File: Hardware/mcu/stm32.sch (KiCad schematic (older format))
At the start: 37 parts, among them P1101 EXP1, P1102 EXP2, P1103 EXP3, P1104 EXP4, P1105 EXPPWR, P901 EXP5, Q1101 NPN, SW1101 Reset, U1101 STM32F103ZC, U903 XO53, X1101 32KHz

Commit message: splitted schematics are ready. MCU/Display board is ready.
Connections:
- net +3.3V: now also P1105.3; no longer P1105.2
- net GND: now also P1105.2, P901.1 (P1); no longer P1105.3
- net PA0 renamed ~FLASH_CS
- net ~FLASH_CS: no longer P901.1 (P1)
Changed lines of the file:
@@
-EESchema Schematic File Version 2  date Do 10 Mär 2011 01:37:58 CET
+EESchema Schematic File Version 2  date Do 10 Mär 2011 16:44:23 CET
 LIBS:power
 LIBS:device
@@
 EELAYER END
 $Descr A3 16535 11700
+encoding utf-8
 Sheet 9 9
 Title ""
-Date "9 mar 2011"
+Date "10 mar 2011"
 Rev ""
 Comp ""
@@
 Comment4 ""
 $EndDescr
+Text HLabel 7000 2450 0    60   Output ~ 0
+~FLASH_CS
+$Comp
+L GND #PWR901
+U 1 1 4D78ED63
+P 1950 4300
+F 0 "#PWR901" H 1950 4300 30  0001 C CNN
+F 1 "GND" H 1950 4230 30  0001 C CNN
+	1    1950 4300
+	0    1    1    0
+$EndComp
 Wire Wire Line
 	4100 7600 4100 7700
@@
 	5200 7700 7000 7700
 $Comp
-L +3.3V #PWR060
+L +3.3V #PWR913
 U 1 1 4D77FF13
 P 4100 7700
-F 0 "#PWR060" H 4100 7660 30  0001 C CNN
+F 0 "#PWR913" H 4100 7660 30  0001 C CNN
 F 1 "+3.3V" H 4100 7810 30  0000 C CNN
 	1    4100 7700
@@
 $EndComp
 $Comp
-L GND #PWR061
+L GND #PWR922
 U 1 1 4D77FF0D
 P 5200 7600
-F 0 "#PWR061" H 5200 7600 30  0001 C CNN
+F 0 "#PWR922" H 5200 7600 30  0001 C CNN
 F 1 "GND" H 5200 7530 30  0001 C CNN
 	1    5200 7600
@@
 $EndComp
 $Comp
-L GND #PWR062
+L GND #PWR908
 U 1 1 4D77ECC6
 P 2750 4300
-F 0 "#PWR062" H 2750 4300 30  0001 C CNN
+F 0 "#PWR908" H 2750 4300 30  0001 C CNN
 F 1 "GND" H 2750 4230 30  0001 C CNN
 	1    2750 4300
@@
 Text Label 1950 4400 2    60   ~ 0
 PA1
-Text Label 1950 4300 2    60   ~ 0
-PA0
 Text Label 7000 2550 2    60   ~ 0
 PA1
-Text Label 7000 2450 2    60   ~ 0
-PA0
 $Comp
 L CONN_12X2 P901
@@
 NoConn ~ 7000 8100
 $Comp
-L GND #PWR063
+L GND #PWR916
 U 1 1 4D751030
 P 4300 2300
-F 0 "#PWR063" H 4300 2300 30  0001 C CNN
+F 0 "#PWR916" H 4300 2300 30  0001 C CNN
 F 1 "GND" H 4300 2230 30  0001 C CNN
 	1    4300 2300
@@
 $EndComp
 $Comp
-L +3.3V #PWR064
+L +3.3V #PWR910
 U 1 1 4D75102E
+P 3500 2300
+F 0 "#PWR910" H 3500 2260 30  0001 C CNN
+F 1 "+3.3V" H 3500 2410 30  0000 C CNN
+	1    3500 2300
+	-1   0    0    1
+$EndComp
+$Comp
+L GND #PWR915
+U 1 1 4D75102A
 P 4300 2200
-F 0 "#PWR064" H 4300 2160 30  0001 C CNN
-F 1 "+3.3V" H 4300 2310 30  0000 C CNN
+F 0 "#PWR915" H 4300 2200 30  0001 C CNN
+F 1 "GND" H 4300 2130 30  0001 C CNN
 	1    4300 2200
-	1    0    0    -1
-$EndComp
-$Comp
-L GND #PWR065
-U 1 1 4D75102A
-P 3500 2300
-F 0 "#PWR065" H 3500 2300 30  0001 C CNN
-F 1 "GND" H 3500 2230 30  0001 C CNN
-	1    3500 2300
-	1    0    0    -1
-$EndComp
-$Comp
-L +3.3V #PWR066
+	0    -1   -1   0
+$EndComp
+$Comp
+L +3.3V #PWR909
 U 1 1 4D751027
 P 3500 2200
-F 0 "#PWR066" H 3500 2160 30  0001 C CNN
+F 0 "#PWR909" H 3500 2160 30  0001 C CNN
 F 1 "+3.3V" H 3500 2310 30  0000 C CNN
 	1    3500 2200
@@
 $EndComp
 $Comp
-L GND #PWR067
+L GND #PWR918
 U 1 1 4D750ECA
 P 4750 5300
-F 0 "#PWR067" H 4750 5300 30  0001 C CNN
+F 0 "#PWR918" H 4750 5300 30  0001 C CNN
 F 1 "GND" H 4750 5230 30  0001 C CNN
 	1    4750 5300
@@
 $EndComp
 $Comp
-L GND #PWR068
+L GND #PWR917
 U 1 1 4D750EC7
 P 4750 5050
-F 0 "#PWR068" H 4750 5050 30  0001 C CNN
+F 0 "#PWR917" H 4750 5050 30  0001 C CNN
 F 1 "GND" H 4750 4980 30  0001 C CNN
 	1    4750 5050
@@
 $EndComp
 $Comp
-L +3.3V #PWR069
+L +3.3V #PWR906
 U 1 1 4D75098C
 P 2700 3400
-F 0 "#PWR069" H 2700 3360 30  0001 C CNN
+F 0 "#PWR906" H 2700 3360 30  0001 C CNN
 F 1 "+3.3V" H 2700 3510 30  0000 C CNN
 	1    2700 3400
@@
 $EndComp
 $Comp
-L GND #PWR070
+L GND #PWR907
 U 1 1 4D75098B
 P 2700 3500
-F 0 "#PWR070" H 2700 3500 30  0001 C CNN
+F 0 "#PWR907" H 2700 3500 30  0001 C CNN
 F 1 "GND" H 2700 3430 30  0001 C CNN
 	1    2700 3500
@@
 $EndComp
 $Comp
-L +3.3V #PWR071
+L +3.3V #PWR912
 U 1 1 4D750989
 P 3750 3600
-F 0 "#PWR071" H 3750 3560 30  0001 C CNN
+F 0 "#PWR912" H 3750 3560 30  0001 C CNN
 F 1 "+3.3V" H 3750 3710 30  0000 C CNN
 	1    3750 3600
@@
 I2C1_SCL
 $Comp
-L GND #PWR072
+L GND #PWR905
 U 1 1 4D7503BC
 P 2700 2100
-F 0 "#PWR072" H 2700 2100 30  0001 C CNN
+F 0 "#PWR905" H 2700 2100 30  0001 C CNN
 F 1 "GND" H 2700 2030 30  0001 C CNN
 	1    2700 2100
@@
 $EndComp
 $Comp
-L +3.3V #PWR073
+L +3.3V #PWR904
 U 1 1 4D7503BA
 P 2700 1800
-F 0 "#PWR073" H 2700 1760 30  0001 C CNN
+F 0 "#PWR904" H 2700 1760 30  0001 C CNN
 F 1 "+3.3V" H 2700 1910 30  0000 C CNN
 	1    2700 1800
@@
 ~EXP1_CS
 $Comp
-L +3.3V #PWR074
+L +3.3V #PWR911
 U 1 1 4D75038D
 P 3750 1250
-F 0 "#PWR074" H 3750 1210 30  0001 C CNN
+F 0 "#PWR911" H 3750 1210 30  0001 C CNN
 F 1 "+3.3V" H 3750 1360 30  0000 C CNN
 	1    3750 1250
@@
 ~EXP1_CS
 $Comp
-L GND #PWR075
+L GND #PWR903
 U 1 1 4D75033D
 P 2700 1150
-F 0 "#PWR075" H 2700 1150 30  0001 C CNN
+F 0 "#PWR903" H 2700 1150 30  0001 C CNN
 F 1 "GND" H 2700 1080 30  0001 C CNN
 	1    2700 1150
@@
 $EndComp
 $Comp
-L +3.3V #PWR076
+L +3.3V #PWR902
 U 1 1 4D75033B
 P 2700 1050
-F 0 "#PWR076" H 2700 1010 30  0001 C CNN
+F 0 "#PWR902" H 2700 1010 30  0001 C CNN
 F 1 "+3.3V" H 2700 1160 30  0000 C CNN
 	1    2700 1050
@@
 Expansion Headers
 $Comp
-L +3.3V #PWR077
+L +3.3V #PWR924
 U 1 1 4D750217
 P 5800 3350
-F 0 "#PWR077" H 5800 3310 30  0001 C CNN
+F 0 "#PWR924" H 5800 3310 30  0001 C CNN
 F 1 "+3.3V" H 5800 3460 30  0000 C CNN
 	1    5800 3350
@@
 $EndComp
 $Comp
-L GND #PWR078
+L GND #PWR921
 U 1 1 4D750205
 P 4950 3000
-F 0 "#PWR078" H 4950 3000 30  0001 C CNN
+F 0 "#PWR921" H 4950 3000 30  0001 C CNN
 F 1 "GND" H 4950 2930 30  0001 C CNN
 	1    4950 3000
@@
 $EndComp
 $Comp
-L +3.3V #PWR079
+L +3.3V #PWR914
 U 1 1 4D7501F6
 P 4150 3950
-F 0 "#PWR079" H 4150 3910 30  0001 C CNN
+F 0 "#PWR914" H 4150 3910 30  0001 C CNN
 F 1 "+3.3V" H 4150 4060 30  0000 C CNN
 	1    4150 3950
@@
 FSMC_A0
 $Comp
-L GND #PWR080
+L GND #PWR929
 U 1 1 4D74F260
 P 7000 9050
-F 0 "#PWR080" H 7000 9050 30  0001 C CNN
+F 0 "#PWR929" H 7000 9050 30  0001 C CNN
 F 1 "GND" H 7000 8980 30  0001 C CNN
 	1    7000 9050
@@
 $EndComp
 $Comp
-L GND #PWR081
+L GND #PWR927
 U 1 1 4D74F258
 P 6200 8400
-F 0 "#PWR081" H 6200 8400 30  0001 C CNN
+F 0 "#PWR927" H 6200 8400 30  0001 C CNN
 F 1 "GND" H 6200 8330 30  0001 C CNN
 	1    6200 8400
@@
 $EndComp
 $Comp
-L GND #PWR082
+L GND #PWR923
 U 1 1 4D74F205
 P 5500 8650
-F 0 "#PWR082" H 5500 8650 30  0001 C CNN
+F 0 "#PWR923" H 5500 8650 30  0001 C CNN
 F 1 "GND" H 5500 8580 30  0001 C CNN
 	1    5500 8650
@@
 $EndComp
 $Comp
-L +3.3V #PWR083
+L +3.3V #PWR925
 U 1 1 4D74F1DC
 P 5950 8450
-F 0 "#PWR083" H 5950 8410 30  0001 C CNN
+F 0 "#PWR925" H 5950 8410 30  0001 C CNN
 F 1 "+3.3V" H 5950 8560 30  0000 C CNN
 	1    5950 8450
@@
 NRST
 $Comp
-L GND #PWR084
+L GND #PWR920
 U 1 1 4D74F196
 P 4900 7350
-F 0 "#PWR084" H 4900 7350 30  0001 C CNN
+F 0 "#PWR920" H 4900 7350 30  0001 C CNN
 F 1 "GND" H 4900 7280 30  0001 C CNN
 	1    4900 7350
@@
 $EndComp
 $Comp
-L GND #PWR085
+L GND #PWR919
 U 1 1 4D74F194
 P 4900 6750
-F 0 "#PWR085" H 4900 6750 30  0001 C CNN
+F 0 "#PWR919" H 4900 6750 30  0001 C CNN
 F 1 "GND" H 4900 6680 30  0001 C CNN
 	1    4900 6750
@@
 $EndComp
 $Comp
-L GND #PWR086
+L GND #PWR926
 U 1 1 4D74F016
 P 6150 7550
-F 0 "#PWR086" H 6150 7550 30  0001 C CNN
+F 0 "#PWR926" H 6150 7550 30  0001 C CNN
 F 1 "GND" H 6150 7480 30  0001 C CNN
 	1    6150 7550
@@
 $EndComp
 $Comp
-L +BATT #PWR087
+L +BATT #PWR928
 U 1 1 4D74F00C
 P 6650 7500
-F 0 "#PWR087" H 6650 7450 20  0001 C CNN
+F 0 "#PWR928" H 6650 7450 20  0001 C CNN
 F 1 "+BATT" H 6650 7600 30  0000 C CNN
 	1    6650 7500
@@
 $EndComp
 $Comp
-L GND #PWR088
+L GND #PWR931
 U 1 1 4D74ED22
 P 8000 9750
-F 0 "#PWR088" H 8000 9750 30  0001 C CNN
+F 0 "#PWR931" H 8000 9750 30  0001 C CNN
 F 1 "GND" H 8000 9680 30  0001 C CNN
 	1    8000 9750
@@
 $EndComp
 $Comp
-L +3.3V #PWR089
+L +3.3V #PWR930
 U 1 1 4D74EC62
 P 8000 1650
-F 0 "#PWR089" H 8000 1610 30  0001 C CNN
+F 0 "#PWR930" H 8000 1610 30  0001 C CNN
 F 1 "+3.3V" H 8000 1760 30  0000 C CNN
 	1    8000 1650
@@
 $EndComp
 $Comp
-L +3.3V #PWR090
+L +3.3V #PWR932
 U 1 1 4D74EC28
 P 9600 600
-F 0 "#PWR090" H 9600 560 30  0001 C CNN
+F 0 "#PWR932" H 9600 560 30  0001 C CNN
 F 1 "+3.3V" H 9600 710 30  0000 C CNN
 	1    9600 600
@@
 $EndComp
 $Comp
-L GND #PWR091
+L GND #PWR933
 U 1 1 4D74EC22
 P 9600 1100
-F 0 "#PWR091" H 9600 1100 30  0001 C CNN
+F 0 "#PWR933" H 9600 1100 30  0001 C CNN
 F 1 "GND" H 9600 1030 30  0001 C CNN
 	1    9600 1100

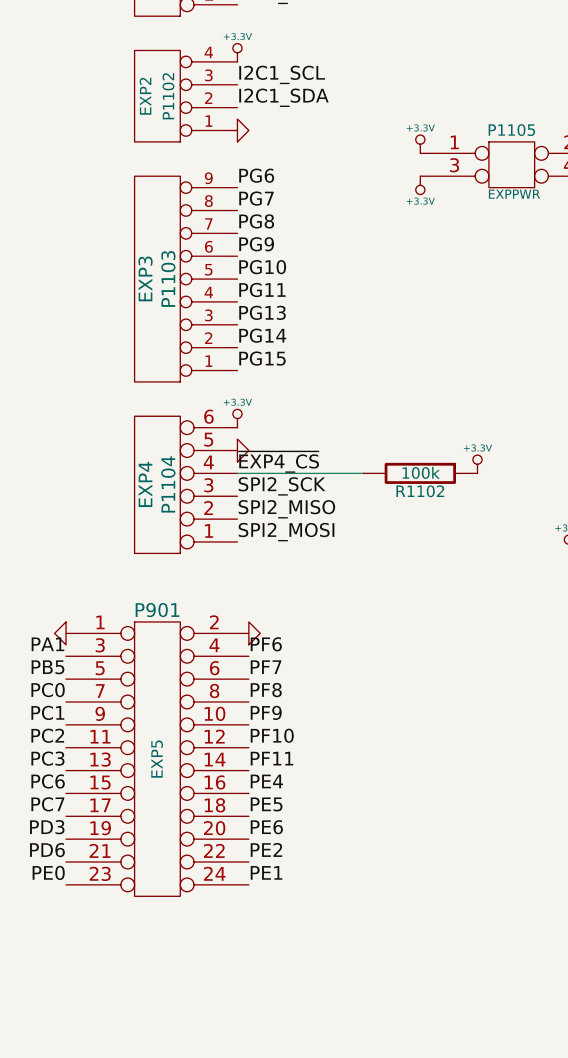
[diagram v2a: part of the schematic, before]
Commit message: using adc instead of analog multiplexer for sensor board, some work on mcu board
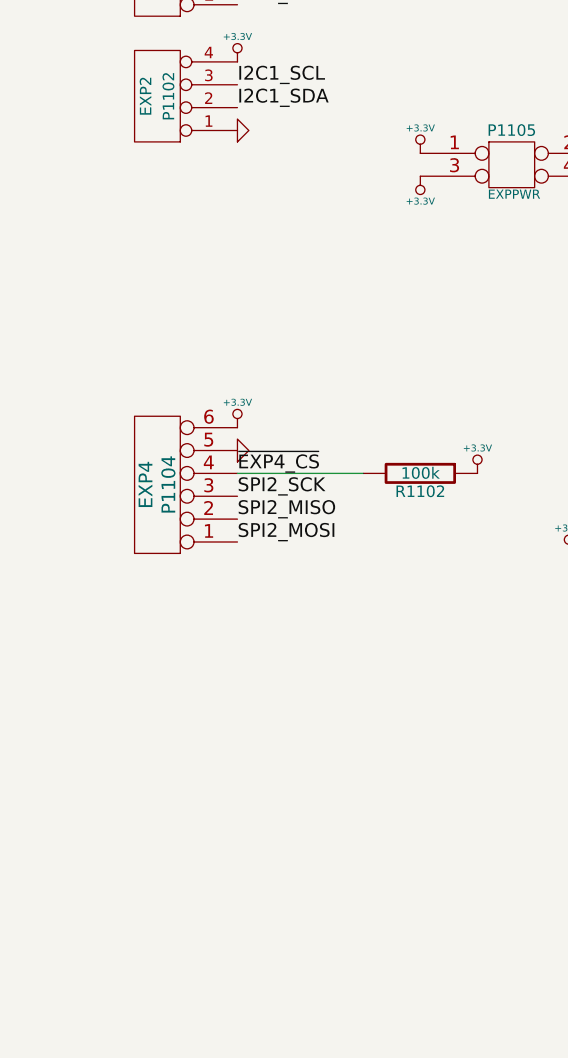
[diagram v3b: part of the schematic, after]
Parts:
- removed P1103: EXP3, symbol CONN_9
- removed P901: EXP5, symbol CONN_12X2
